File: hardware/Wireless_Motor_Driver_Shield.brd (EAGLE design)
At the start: 59.7 x 53.3 mm, 84 parts, among them Q1 MOSFET-NCHANNELBSS138, Q2 MOSFET-NCHANNELBSS138, U1 XBEE-1XBEE-1_LOCK, U2 ARDUINO, U3 TB6612FNG

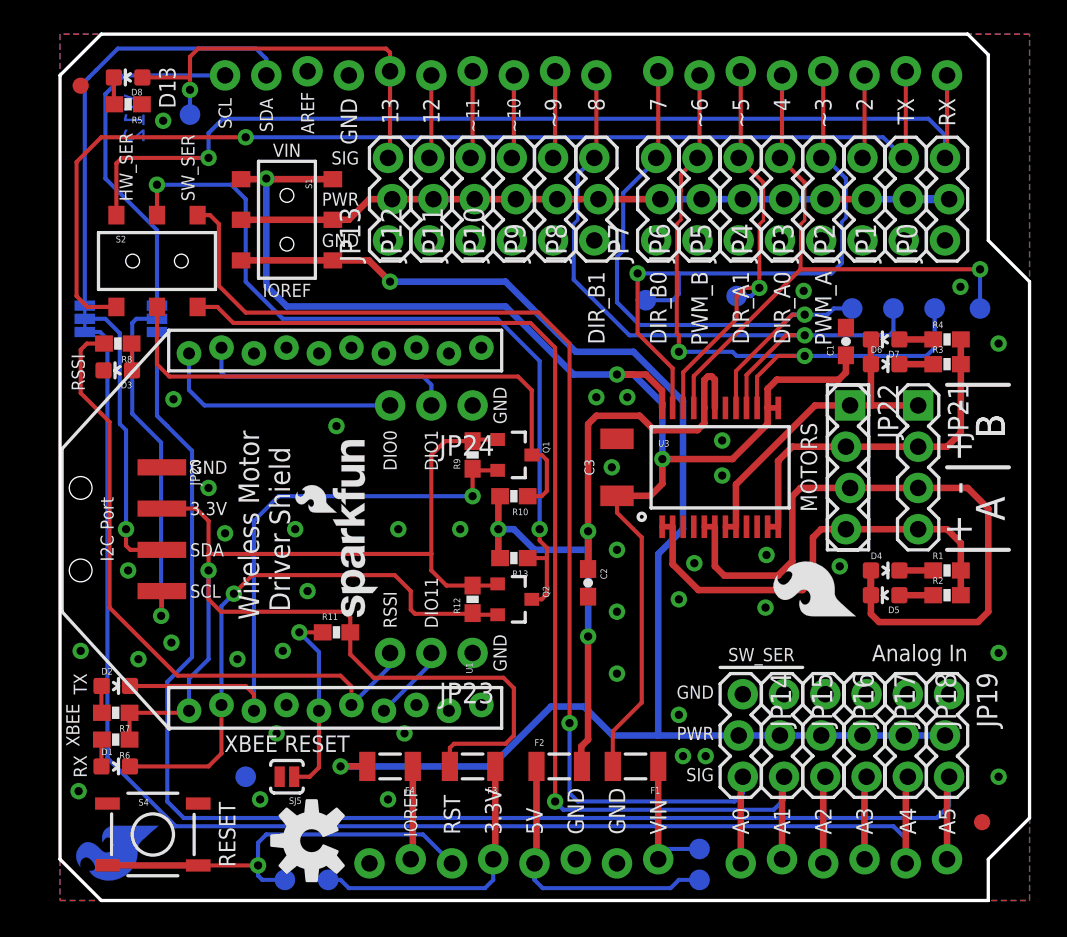
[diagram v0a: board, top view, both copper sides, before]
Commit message: Updated after self Eng Design Rules Check
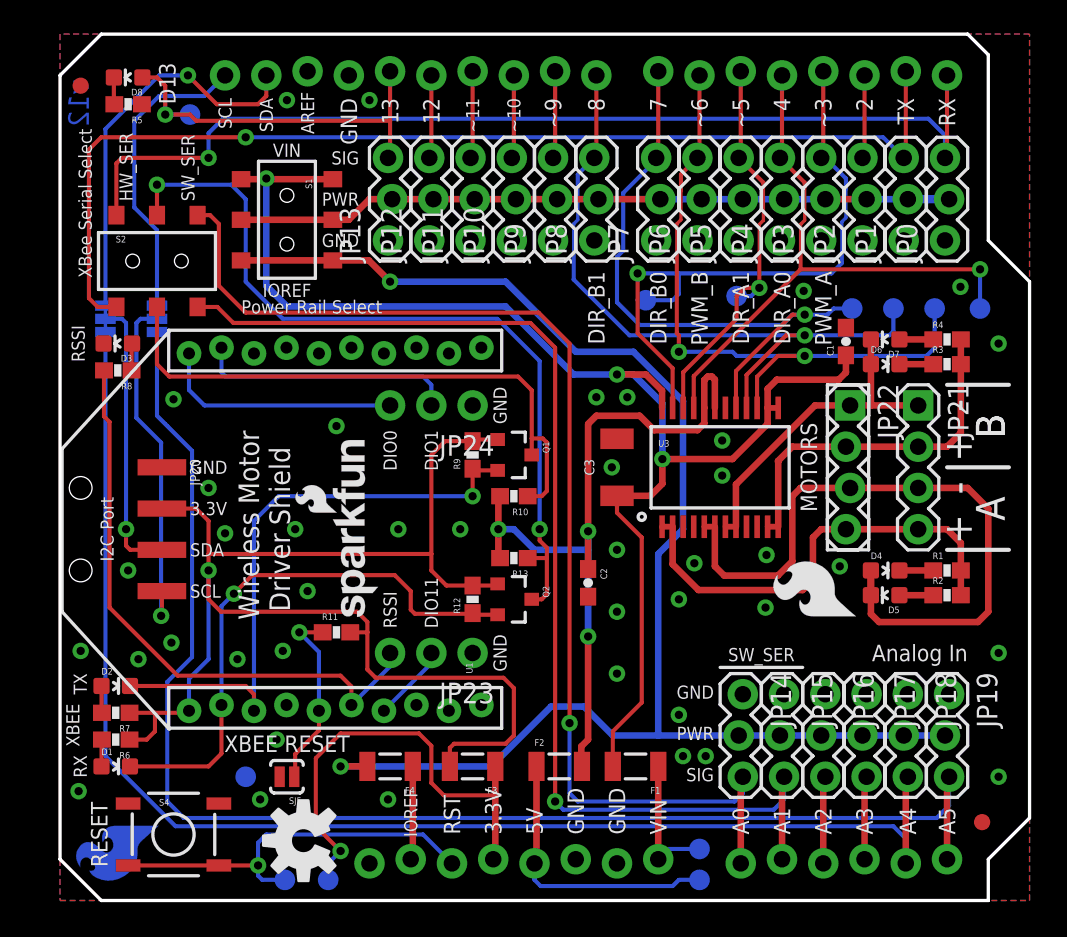
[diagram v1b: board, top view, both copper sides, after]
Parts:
- D1: value Red -> Yellow
- D3: value Yellow -> Red
- moved D3 1.65 mm to (3.56, 34.3)
- moved R8 1.65 mm to (3.56, 32.6)
- moved S4 1.27 mm to (6.99, 4.06)
- moved SJ3 1.27 mm to (2.79, 35.8)
- moved LOGO1 0.51 mm to (15.0, 3.68)
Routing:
- net 3.3V: track 17.6 -> 28.8 mm, vias 0 -> 1
- net SCL: track 22.2 -> 18.7 mm
- net RSSI: track 40.4 -> 37.0 mm
- net SDA: track 27.1 -> 24.4 mm, vias 0 -> 1
- net FUSED_3.3V: track 83.0 -> 85.7 mm
- net D13: track 25.7 -> 24.3 mm
- net RESET: track 25.9 -> 24.7 mm
- net A4: track 85.6 -> 84.5 mm
- net XBEE_TXO: track 35.5 -> 36.6 mm
- net D1/TXO: track 69.4 -> 68.3 mm
- net SDA_I2C_PORT: track 18.1 -> 17.4 mm
- net XBEE_RESET: track 12.0 -> 11.5 mm
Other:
- board text added: "Power Rail Select"
- board text added: "Revised by: Shawn Hymel"
- board text added: "XBee Serial Select"
- board text added: "v12"
- board text removed: "Modified by: Shawn Hymel"
- board text removed: "V12"

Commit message: Added new monster voltage select circuit to servo power rail
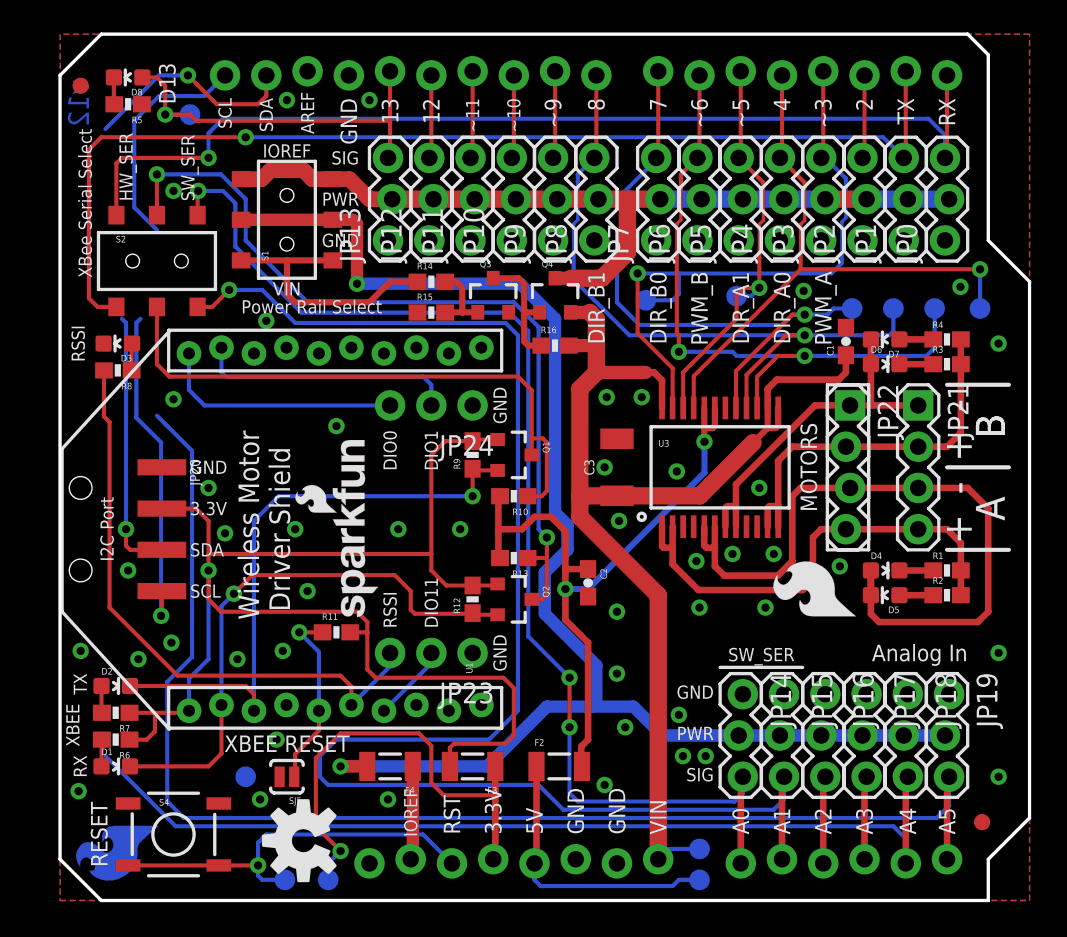
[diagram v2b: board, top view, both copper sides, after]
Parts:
- removed F1: (no value), SparkFun-PowerIC:PTC-1206
- removed SJ3, SJ4: (no value), SparkFun-Passives:PAD-JUMPER-3-3OF3_NC_BY_TRACE_YES_SILK_FULL_BOX
- added Q3: MMBT2222A, SparkFun-DiscreteSemi:SOT23-3
- added Q4: DMG2307L, SparkFun-DiscreteSemi:SOT23-3
- added R14: 1K, SparkFun-Resistors:0603-RES
- added R15, R16: 10K, SparkFun-Resistors:0603-RES
- D2: value Green -> GREEN
- D3: value Red -> RED
- D8: value Blue -> GREEN
- turned S1 to 90 degrees
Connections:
- removed net FUSED_VIN: C1.1, C3.1, F1.2, S1.1, S1.4, U3.13, U3.14, U3.24
- removed net SCL_I2C_PORT: JP20.4, SJ4.2
- removed net SDA_I2C_PORT: JP20.3, SJ3.2
- new net N$11: Q3.3, Q4.1, R16.1
- new net N$13: R14.1, S1.1, S1.4
- new net N$2: Q3.1, R14.2, R15.2
- net A4: no longer SJ3.3
- net A5: no longer SJ4.3
- net FUSED_IOREF: now also S1.2, S1.5; no longer S1.3, S1.6
- net GND: now also Q3.2, R15.1
- net PWR_RAIL: now also Q4.3, S1.3, S1.6; no longer S1.2, S1.5
- net SCL: now also JP20.4; no longer SJ4.1
- net SDA: now also JP20.3; no longer SJ3.1
- net VIN: now also C1.1, C3.1, Q4.2, R16.2, U3.13, U3.14, U3.24; no longer F1.1
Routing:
- net FUSED_VIN: track 86.5 -> 0.00 mm, vias 3 -> 0
- net VIN: track 8.52 -> 71.8 mm
- net A4: track 84.5 -> 58.4 mm
- net A1/SW_TXO: track 72.1 -> 95.3 mm
- net SCL_I2C_PORT: track 21.6 -> 0.00 mm, vias 1 -> 0
- net SDA_I2C_PORT: track 17.4 -> 0.00 mm, vias 1 -> 0
- net N$13: track 0.00 -> 16.5 mm
- net SCL: track 18.7 -> 34.6 mm, vias 0 -> 1
- net PWR_RAIL: track 44.1 -> 53.0 mm
- net N$11: track 0.00 -> 7.76 mm
- net SDA: track 24.4 -> 29.9 mm, vias 1 -> 2
- net A5: track 86.2 -> 81.1 mm
- net N$2: track 0.00 -> 4.74 mm
- net FUSED_5V: track 46.7 -> 42.7 mm, vias 3 -> 2
- net FUSED_IOREF: track 93.1 -> 91.3 mm
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
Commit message: Added fiducials, cleaned up silk, added staking vias
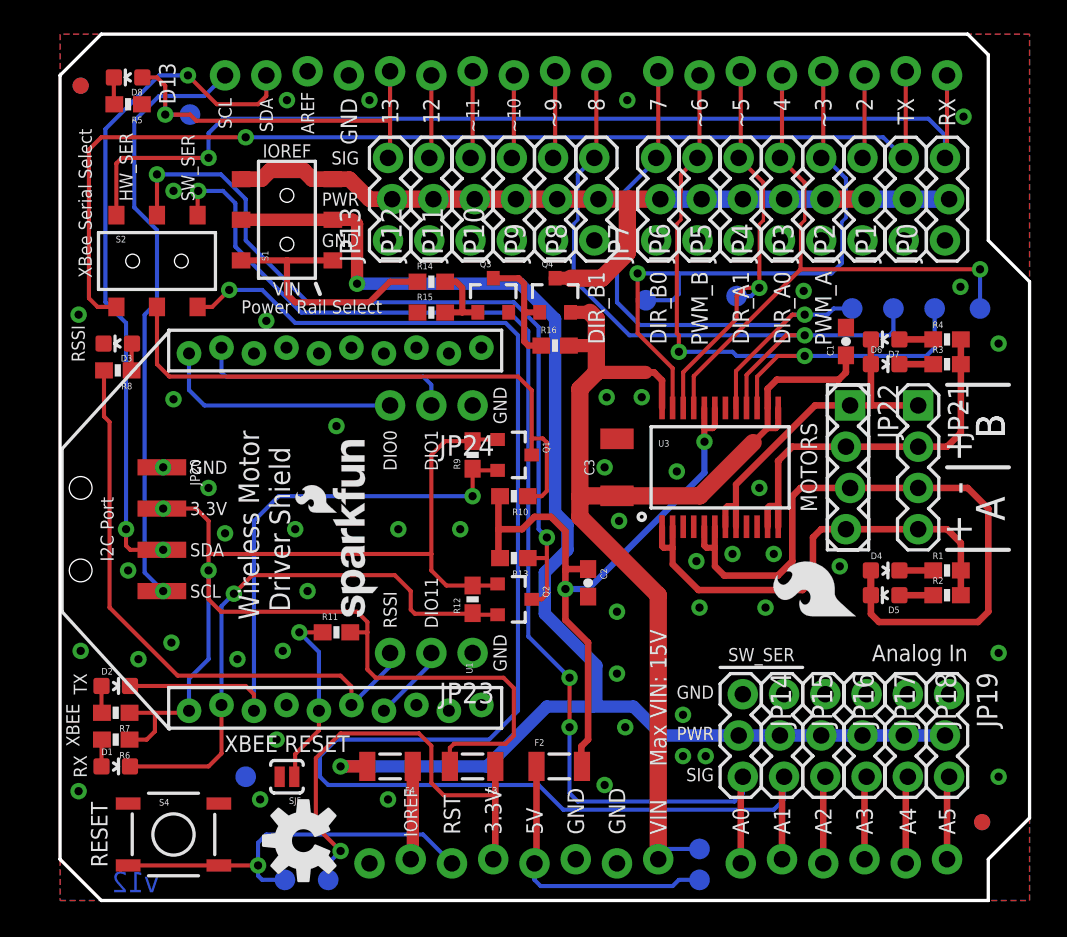
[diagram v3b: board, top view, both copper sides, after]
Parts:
- removed LOGO5: SFE_LOGO_FLAME.2COP, SparkFun-Aesthetics:SFE_LOGO_FLAME_COPPER_.2
- added FID3, FID4: FIDUCIAL1X2, SparkFun-Aesthetics:FIDUCIAL-1X2
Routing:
- net A5: track 81.1 -> 5.13 mm
- net A4: track 58.4 -> 5.39 mm
- net SDA: track 29.9 -> 42.1 mm, vias 2 -> 3
- net SCL: track 34.6 -> 37.1 mm
- net FUSED_3.3V: vias 1 -> 2
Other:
- board text added: "Max VIN: 15V"

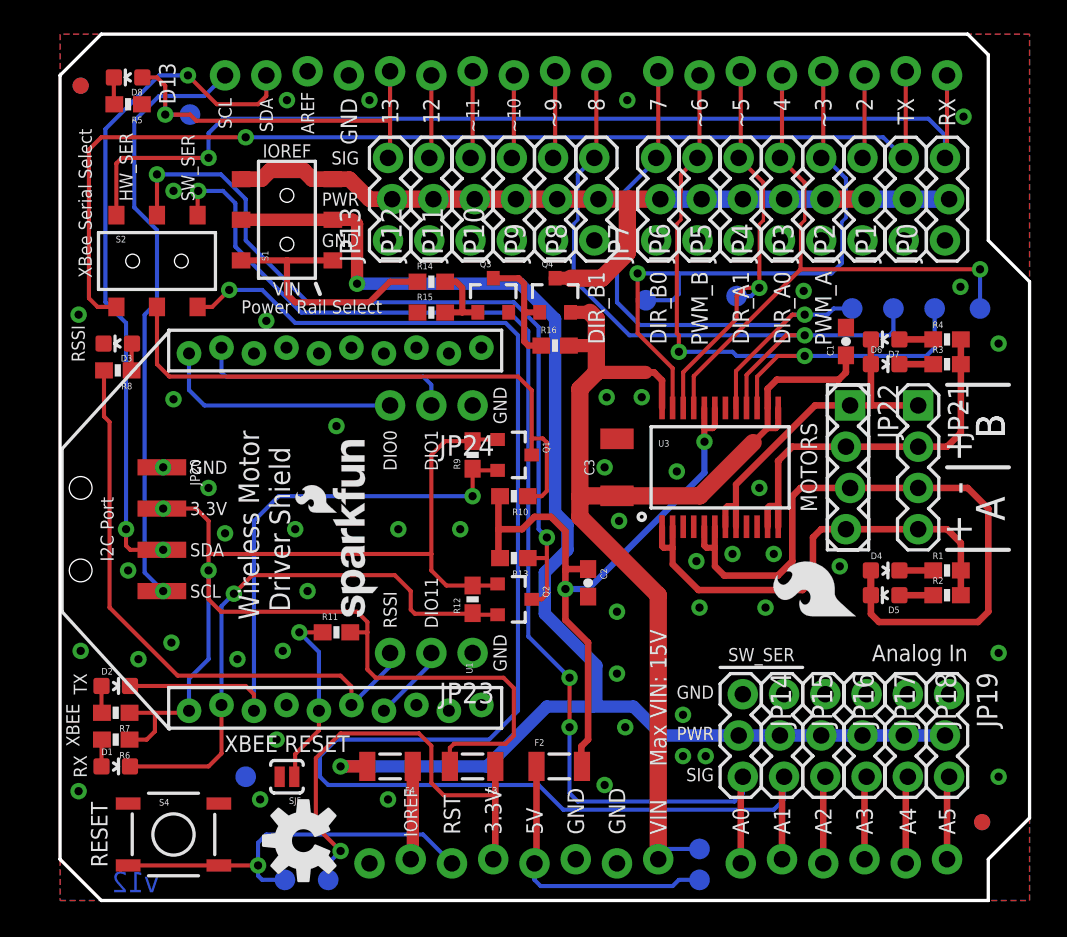
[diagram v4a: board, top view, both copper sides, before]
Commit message: Added female I2C header. Added manual selector switch for VIN/VS with new barrel jack to power motors separately.
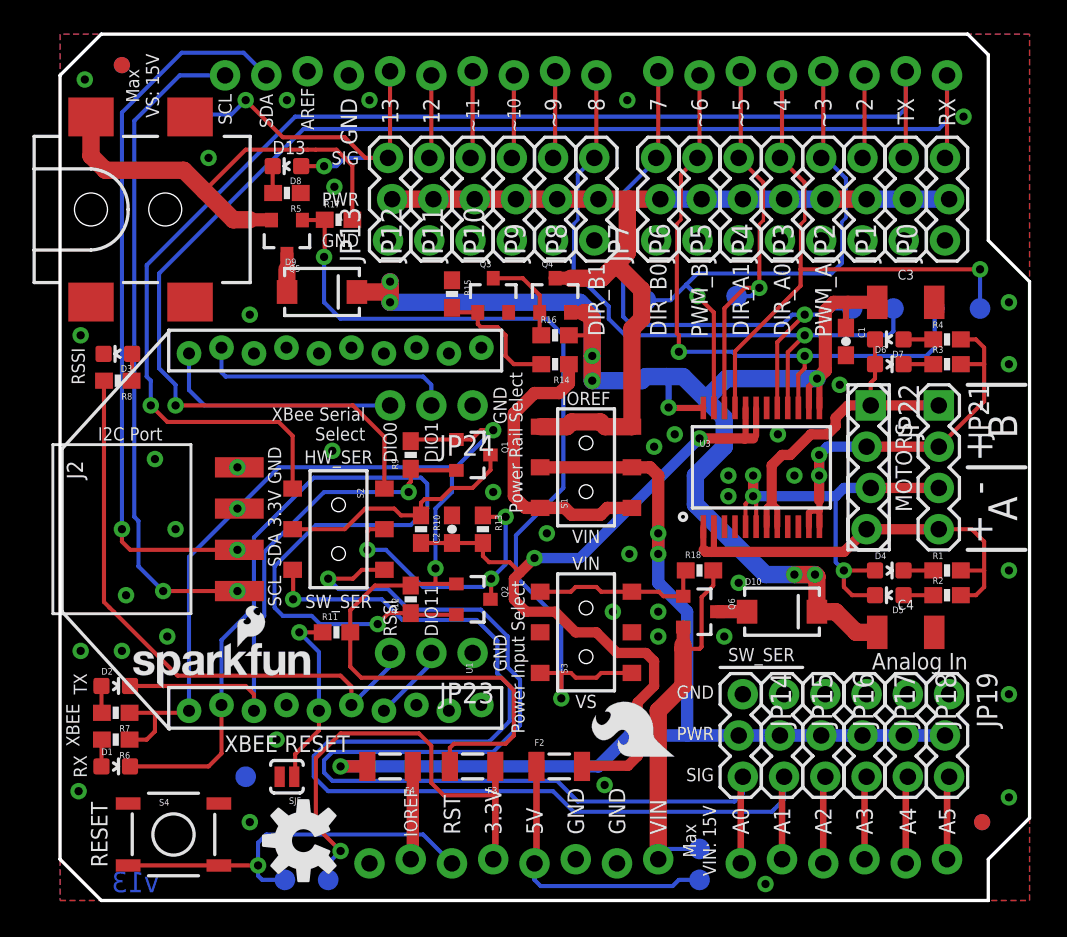
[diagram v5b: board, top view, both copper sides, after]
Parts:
- removed JP20: (no value), SparkFun-Connectors:1X04_SMD_RA_MALE
- added C4: 10uF, SparkFun-Capacitors:1210
- added D10, D9: B340A, SparkFun-DiscreteSemi:SMA-DIODE
- added J1: 5.5x2.1mm Barrel, SparkFun-Connectors:POWER_JACK_SMD
- added J2: (no value), SparkFun-Connectors:1X04_SMD_RA_FEMALE
- added Q5, Q6: DMG2307L, SparkFun-DiscreteSemi:SOT23-3
- added R17, R18: 10K, SparkFun-Resistors:0603-RES
- added S3: (no value), SparkFun-Electromechanical:AYZ0202
- JP21: device SparkFun-Connectors:1X04@1 -> SparkFun-Connectors:1X04
- JP22: device SparkFun-Connectors:1X04_LOCK@1 -> SparkFun-Connectors:1X04_LOCK
- moved LOGO4 37.2 mm to (54.0, 13.8), turned to 0 degrees
- moved S1 23.9 mm to (32.4, 26.7)
- moved C3 20.5 mm to (52.1, 36.8), turned to 0 degrees
- moved S2 19.9 mm to (17.1, 22.9), turned to 270 degrees
- moved LOGO2 16.1 mm to (4.06, 13.0), turned to 0 degrees
- moved LOGO3 14.1 mm to (38.1, 8.51)
- moved D8 11.2 mm to (14.0, 45.2)
- moved R5 11.2 mm to (14.0, 43.6)
- moved R14 9.16 mm to (30.5, 33.0), turned to 180 degrees
- moved C2 9.01 mm to (24.1, 22.9), turned to 90 degrees
- moved R10 6.07 mm to (22.2, 22.9), turned to 270 degrees
- moved R12 3.81 mm to (21.6, 18.5)
- moved R9 3.81 mm to (21.6, 27.4)
- moved FID1 2.84 mm to (3.81, 51.4)
- moved FID3 2.84 mm to (3.81, 51.4)
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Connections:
- new net N$10: J1.VIN0, Q5.2, R17.2
- new net N$12: Q5.1, R17.1, S3.1, S3.4
- new net N$15: D9.A, Q5.3
- new net N$16: D10.A, Q6.3
- new net N$4: Q6.1, R18.1, S3.3, S3.6
- new net VMOTOR: C1.1, C3.1, C4.1, D10.C, D9.C, Q4.2, R16.2, U3.13, U3.14, U3.24
- net FUSED_3.3V: now also J2.2; no longer JP20.2
- net GND: now also C4.2, J1.GND, J2.1, S3.2, S3.5; no longer JP20.1
- net SCL: now also J2.4; no longer JP20.4
- net SDA: now also J2.3; no longer JP20.3
- net VIN: now also Q6.2, R18.2; no longer C1.1, C3.1, Q4.2, R16.2, U3.13, U3.14, U3.24
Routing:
- net VMOTOR: track 0.00 -> 85.5 mm, vias 0 -> 8
- net N$12: track 0.00 -> 54.2 mm, vias 0 -> 2
- net VIN: track 71.8 -> 23.9 mm
- net XBEE_RXI: track 50.3 -> 17.9 mm, vias 2 -> 3
- net N$10: track 0.00 -> 29.1 mm
- net FUSED_IOREF: track 91.3 -> 65.1 mm, vias 2 -> 3
- net DOUT: track 34.5 -> 59.3 mm
- net A1/SW_TXO: track 95.3 -> 71.6 mm
- net D0/RXI: track 63.2 -> 85.7 mm
- net XBEE_TXO: track 36.6 -> 15.4 mm
- net AOUT2: track 44.7 -> 28.0 mm, vias 0 -> 3
- net D1/TXO: track 68.3 -> 79.9 mm
- net N$4: track 0.00 -> 10.8 mm
- net FUSED_5V: track 42.7 -> 51.0 mm
- net PWR_RAIL: track 53.0 -> 59.5 mm
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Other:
- board text added: "Max VS: 15V"
- board text added: "Power Input Select"
- board text added: "VS"
- board text added: "v13"
- board text removed: "v12"
